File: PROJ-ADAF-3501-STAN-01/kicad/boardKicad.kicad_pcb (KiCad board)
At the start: 16 copper layers, 28 x 27.5 mm, 29 parts, among them CN1 JST-PH, IC1 ATSAMD21E, Q1 reset, SW1 EG1218, U1 AP2112K-3.3, X2 MicroUSB

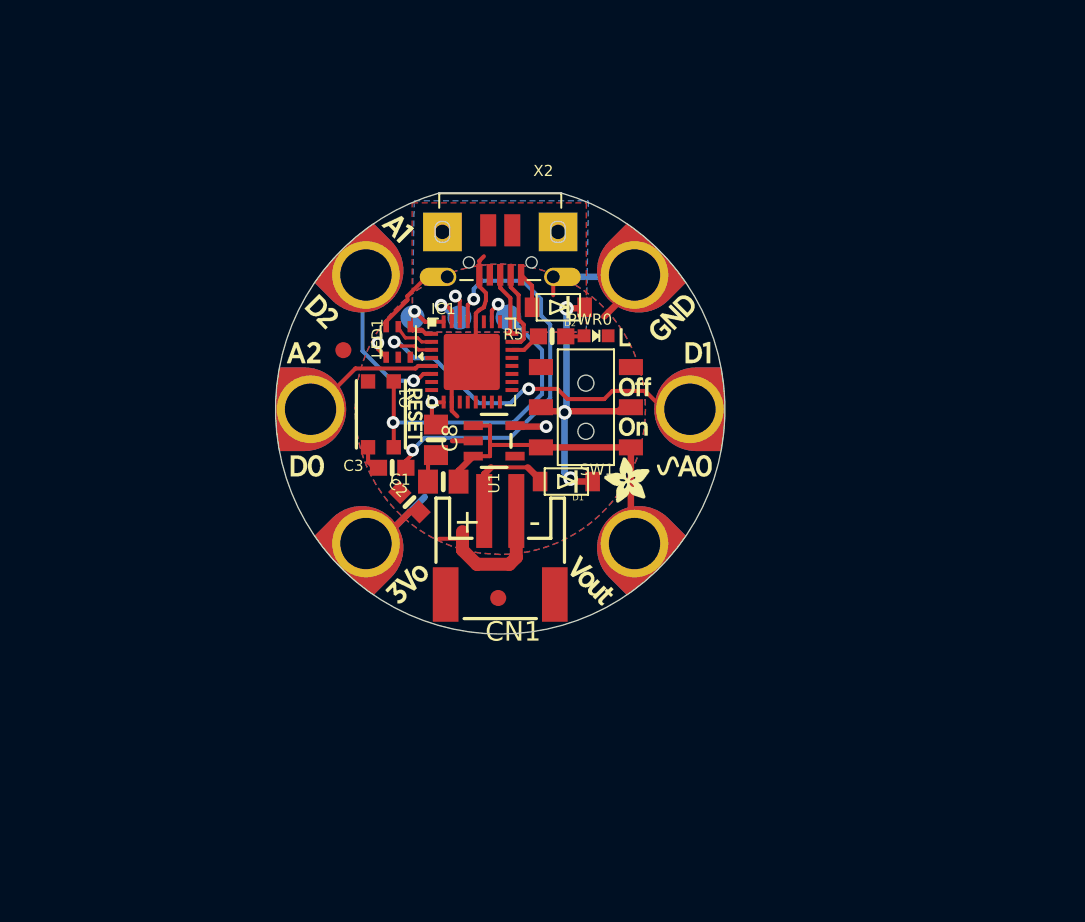
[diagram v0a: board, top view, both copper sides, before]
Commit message: Added a bounding box
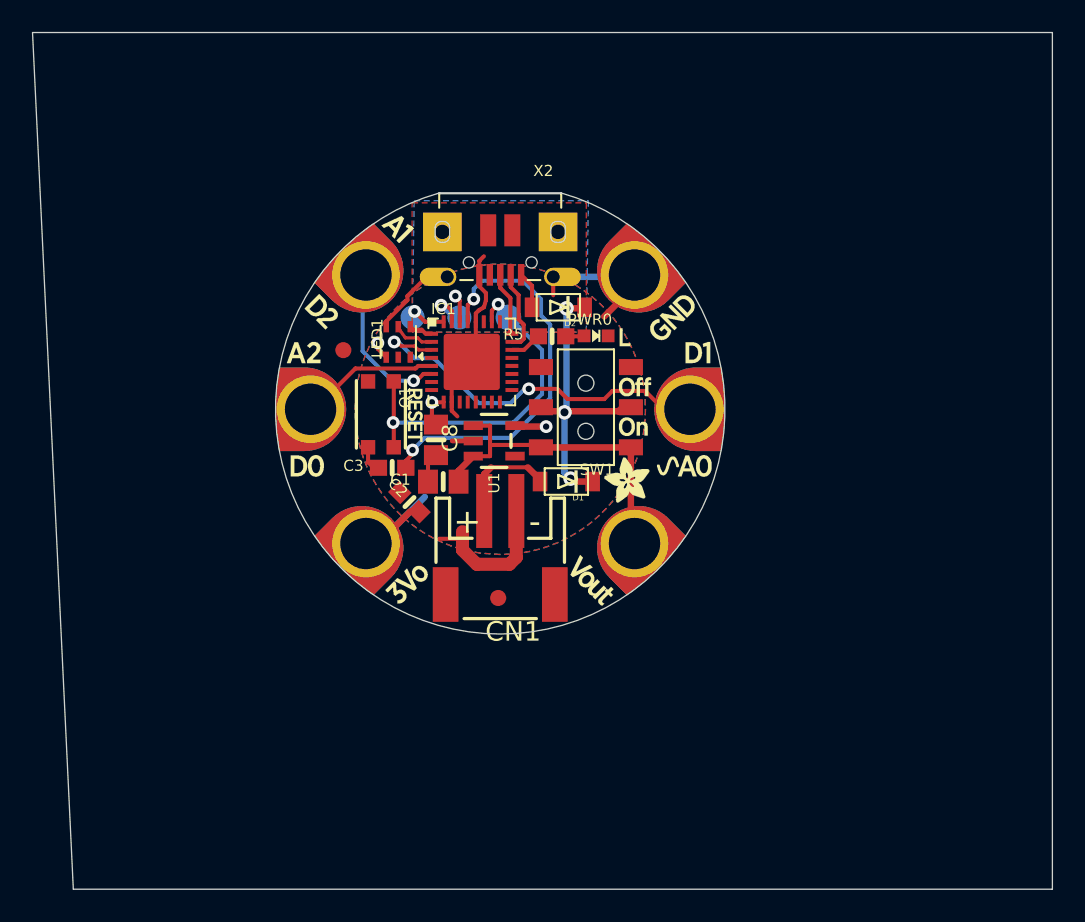
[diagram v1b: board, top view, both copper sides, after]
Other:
- board size 28 x 27.5 mm -> 63.5 x 53.3 mm
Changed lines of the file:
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@@
     (fp_line (start 0.4 -0.35) (end 0.4 0.35) (layer "F.Fab") (width 0.1016))
     (fp_line (start -0.4 -0.375) (end -0.4 0.35) (layer "F.Fab") (width 0.1016))
-    (fp_arc (start 0.3 -0.799998) (mid -0.000001 -0.524966) (end -0.3 -0.8) (layer "F.Fab") (width 0.1016))
+    (fp_arc (start 0.3 -0.799998) (mid -0.000001 -0.524967) (end -0.3 -0.8) (layer "F.Fab") (width 0.1016))
     (fp_arc (start -0.275 0.825) (mid 0 0.55) (end 0.275 0.825) (layer "F.Fab") (width 0.0508))
     (fp_circle (center -0.35 -0.625) (end -0.275 -0.625) (layer "F.Fab") (width 0.0508) (fill none))
@@
       (net 9 "SWDIO") (solder_mask_margin 0.0508))
   )
+  (gr_line (start 182.88 81.28) (end 182.88 134.62) (layer "Edge.Cuts") (width 0.05))
+  (gr_line (start 182.88 134.62) (end 121.92 134.62) (layer "Edge.Cuts") (width 0.05))
+  (gr_line (start 119.38 81.28) (end 182.88 81.28) (layer "Edge.Cuts") (width 0.05))
+  (gr_line (start 121.92 134.62) (end 119.38 81.28) (layer "Edge.Cuts") (width 0.05))
   (gr_line (start 144.6911 91.275005) (end 152.3111 91.275005) (layer "Edge.Cuts") (width 0.05))
   (gr_arc (start 152.3111 91.275005) (mid 148.5011 118.732194) (end 144.6911 91.275005) (layer "Edge.Cuts") (width 0.05))
